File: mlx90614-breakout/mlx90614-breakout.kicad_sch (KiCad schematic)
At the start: 7 parts, among them J1 Conn_01x04_Male, U1 MLX90614

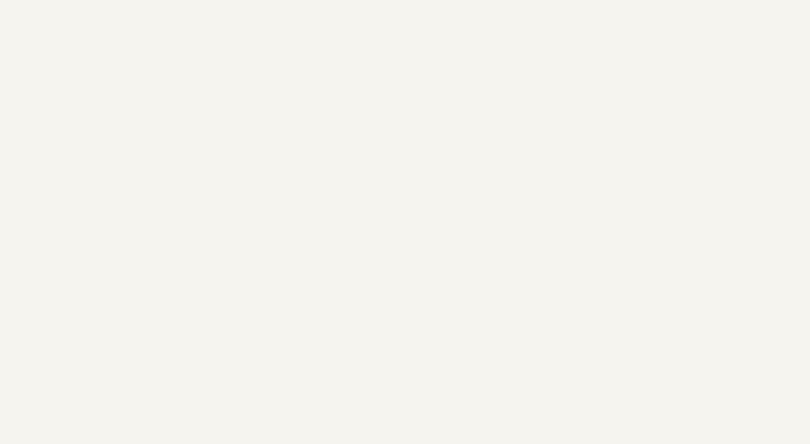
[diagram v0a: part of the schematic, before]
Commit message: updated breakout boards
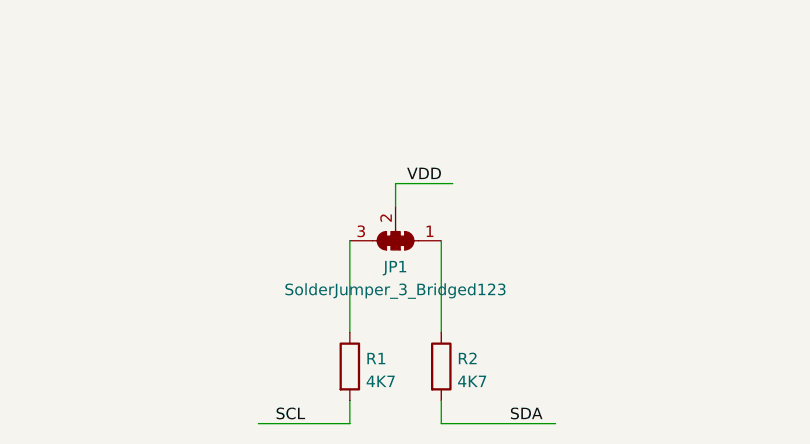
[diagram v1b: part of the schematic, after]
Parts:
- added JP1: SolderJumper_3_Bridged123, Jumper:SolderJumper-3_P1.3mm_Bridged12_RoundedPad1.0x1.5mm_NumberLabels, symbol Jumper:SolderJumper_3_Bridged123
- added R1, R2: 4K7, Resistor_SMD:R_0805_2012Metric, symbol Device:R
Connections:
- net SCL: now also R1.2
- net SDA: now also R2.2
- net VDD: now also JP1.2 (C)
- new net: JP1.1 (A), R2.1
- new net: JP1.3 (B), R1.1
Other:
- company: (none) -> Melexis Inc
- title: (none) -> mlx90614-breakout
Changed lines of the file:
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@@
 (kicad_sch (version 20211123) (generator eeschema)
   (paper "A3")
+  (title_block
+    (title "mlx90614-breakout")
+    (date "2023-01-13")
+    (rev "1.2")
+    (company "Melexis Inc")
+  )
   (junction (at 137.16 61.595) (diameter 0) (color 0 0 0 0)
   )
@@
     (stroke (width 0) (type default) (color 0 0 0 0))
   )
+  (wire (pts (xy 138.43 135.89) (xy 138.43 138.43))
+    (stroke (width 0) (type default) (color 0 0 0 0))
+  )
   (wire (pts (xy 137.16 61.595) (xy 125.73 61.595))
     (stroke (width 0) (type default) (color 0 0 0 0))
@@
     (stroke (width 0) (type default) (color 0 0 0 0))
   )
+  (wire (pts (xy 148.59 135.89) (xy 148.59 138.43))
+    (stroke (width 0) (type default) (color 0 0 0 0))
+  )
+  (wire (pts (xy 148.59 138.43) (xy 161.29 138.43))
+    (stroke (width 0) (type default) (color 0 0 0 0))
+  )
   (wire (pts (xy 204.47 59.055) (xy 204.47 59.69))
     (stroke (width 0) (type default) (color 0 0 0 0))
@@
     (stroke (width 0) (type default) (color 0 0 0 0))
   )
+  (wire (pts (xy 148.59 118.11) (xy 148.59 128.27))
+    (stroke (width 0) (type default) (color 0 0 0 0))
+  )
+  (wire (pts (xy 138.43 118.11) (xy 138.43 128.27))
+    (stroke (width 0) (type default) (color 0 0 0 0))
+  )
+  (wire (pts (xy 128.27 138.43) (xy 138.43 138.43))
+    (stroke (width 0) (type default) (color 0 0 0 0))
+  )
   (wire (pts (xy 204.47 72.39) (xy 204.47 73.66))
     (stroke (width 0) (type default) (color 0 0 0 0))
@@
     (stroke (width 0) (type default) (color 0 0 0 0))
   )
+  (wire (pts (xy 143.51 114.3) (xy 143.51 111.76))
+    (stroke (width 0) (type default) (color 0 0 0 0))
+  )
   (wire (pts (xy 144.78 86.36) (xy 204.47 86.36))
     (stroke (width 0) (type default) (color 0 0 0 0))
   )
+  (wire (pts (xy 143.51 111.76) (xy 149.86 111.76))
+    (stroke (width 0) (type default) (color 0 0 0 0))
+  )
   (wire (pts (xy 59.944 121.92) (xy 78.994 121.92))
     (stroke (width 0) (type default) (color 0 0 0 0))
@@
     (effects (font (size 1.27 1.27)) (justify left bottom))
   )
+  (label "SCL" (at 130.175 138.43 0)
+    (effects (font (size 1.27 1.27)) (justify left bottom))
+  )
   (label "SCL" (at 127 61.595 0)
     (effects (font (size 1.27 1.27)) (justify left bottom))
@@
     (effects (font (size 1.27 1.27)) (justify left bottom))
   )
+  (label "VDD" (at 144.78 111.76 0)
+    (effects (font (size 1.27 1.27)) (justify left bottom))
+  )
   (label "VDD" (at 69.85 121.92 0)
+    (effects (font (size 1.27 1.27)) (justify left bottom))
+  )
+  (label "SDA" (at 156.21 138.43 0)
     (effects (font (size 1.27 1.27)) (justify left bottom))
   )
@@
     (pin "4")
   )
+  (symbol (lib_id "Jumper:SolderJumper_3_Bridged123") (at 143.51 118.11 180) (unit 1)
+    (in_bom yes) (on_board yes) (fields_autoplaced)
+    (property "Reference" "JP1" (id 0) (at 143.51 121.0294 0))
+    (property "Value" "SolderJumper_3_Bridged123" (id 1) (at 143.51 123.5663 0))
+    (property "Footprint" "Jumper:SolderJumper-3_P1.3mm_Bridged12_RoundedPad1.0x1.5mm_NumberLabels" (id 2) (at 143.51 118.11 0)
+      (effects (font (size 1.27 1.27)) hide)
+    )
+    (property "Datasheet" "~" (id 3) (at 143.51 118.11 0)
+      (effects (font (size 1.27 1.27)) hide)
+    )
+    (pin "1")
+    (pin "2")
+    (pin "3")
+  )
+  (symbol (lib_id "Device:R") (at 148.59 132.08 0) (unit 1)
+    (in_bom yes) (on_board yes) (fields_autoplaced)
+    (property "Reference" "R2" (id 0) (at 150.368 131.2453 0)
+      (effects (font (size 1.27 1.27)) (justify left))
+    )
+    (property "Value" "4K7" (id 1) (at 150.368 133.7822 0)
+      (effects (font (size 1.27 1.27)) (justify left))
+    )
+    (property "Footprint" "Resistor_SMD:R_0805_2012Metric" (id 2) (at 146.812 132.08 90)
+      (effects (font (size 1.27 1.27)) hide)
+    )
+    (property "Datasheet" "~" (id 3) (at 148.59 132.08 0)
+      (effects (font (size 1.27 1.27)) hide)
+    )
+    (pin "1")
+    (pin "2")
+  )
+  (symbol (lib_id "Device:R") (at 138.43 132.08 0) (unit 1)
+    (in_bom yes) (on_board yes) (fields_autoplaced)
+    (property "Reference" "R1" (id 0) (at 140.208 131.2453 0)
+      (effects (font (size 1.27 1.27)) (justify left))
+    )
+    (property "Value" "4K7" (id 1) (at 140.208 133.7822 0)
+      (effects (font (size 1.27 1.27)) (justify left))
+    )
+    (property "Footprint" "Resistor_SMD:R_0805_2012Metric" (id 2) (at 136.652 132.08 90)
+      (effects (font (size 1.27 1.27)) hide)
+    )
+    (property "Datasheet" "~" (id 3) (at 138.43 132.08 0)
+      (effects (font (size 1.27 1.27)) hide)
+    )
+    (pin "1")
+    (pin "2")
+  )
   (sheet_instances
     (path "/" (page "1"))
@@
       (reference "J1") (unit 1) (value "Conn_01x04_Male") (footprint "melexis-temperature:QWIIC_STEMMA_QT")
     )
+    (path "/5f3281aa-90f2-4ad4-8657-a16f4e0e58ed"
+      (reference "JP1") (unit 1) (value "SolderJumper_3_Bridged123") (footprint "Jumper:SolderJumper-3_P1.3mm_Bridged12_RoundedPad1.0x1.5mm_NumberLabels")
+    )
+    (path "/ecbf60c2-96f9-428f-bb38-b232f6ce50cc"
+      (reference "R1") (unit 1) (value "4K7") (footprint "Resistor_SMD:R_0805_2012Metric")
+    )
+    (path "/703424ab-e58f-43a8-a715-062d84faadc9"
+      (reference "R2") (unit 1) (value "4K7") (footprint "Resistor_SMD:R_0805_2012Metric")
+    )
     (path "/00000000-0000-0000-0000-00005ee38167"
